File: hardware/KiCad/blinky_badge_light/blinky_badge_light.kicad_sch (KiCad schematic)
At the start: 14 parts, among them U1 ESP32-S3-WROOM-1

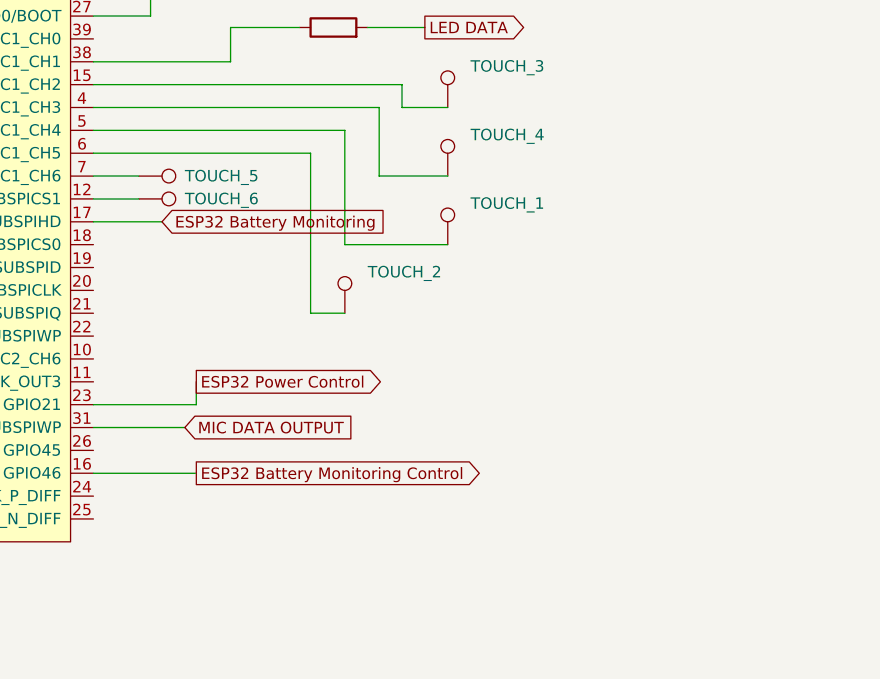
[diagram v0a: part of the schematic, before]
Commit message: adding a bunch of qs and annotated items on schematic
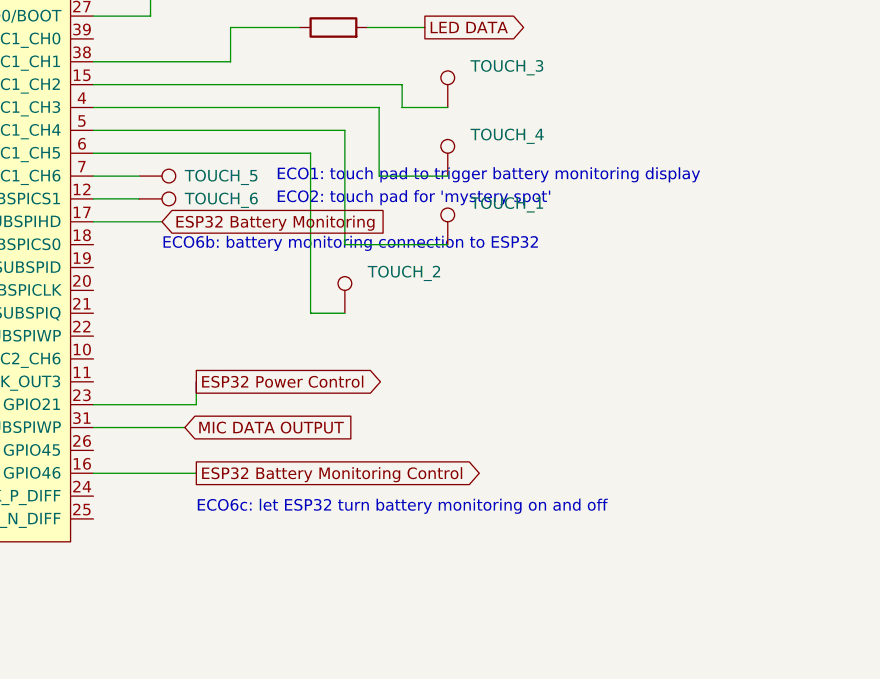
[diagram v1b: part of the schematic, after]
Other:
- note added: "ECO1: touch pad to trigger battery monitoring display"
- note added: "ECO2: touch pad for 'mystery spot'"
- note added: "ECO6b: battery monitoring connection to ESP32"
- note added: "ECO6c: let ESP32 turn battery monitoring on and off"
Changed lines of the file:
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@@
 	(generator_version "9.0")
 	(paper "A4")
+	(text "ECO2: touch pad for 'mystery spot'"
+		(exclude_from_sim yes)
+		(at 212.09 95.25 0)
+		(effects
+			(font
+				(size 1.27 1.27)
+				(color 119 0 255 1)
+			)
+			(justify left)
+		)
+	)
+	(text "ECO1: touch pad to trigger battery monitoring display"
+		(exclude_from_sim yes)
+		(at 212.09 92.71 0)
+		(effects
+			(font
+				(size 1.27 1.27)
+				(color 123 0 255 1)
+			)
+			(justify left)
+		)
+	)
+	(text "ECO6c: let ESP32 turn battery monitoring on and off\n"
+		(exclude_from_sim yes)
+		(at 203.2 129.54 0)
+		(effects
+			(font
+				(size 1.27 1.27)
+				(color 119 0 255 1)
+			)
+			(justify left)
+		)
+	)
+	(text "ECO6b: battery monitoring connection to ESP32"
+		(exclude_from_sim yes)
+		(at 199.39 100.33 0)
+		(effects
+			(font
+				(size 1.27 1.27)
+				(color 119 0 255 1)
+			)
+			(justify left)
+		)
+	)
 	(junction
 		(at 224.79 68.58)

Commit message: remove text from review
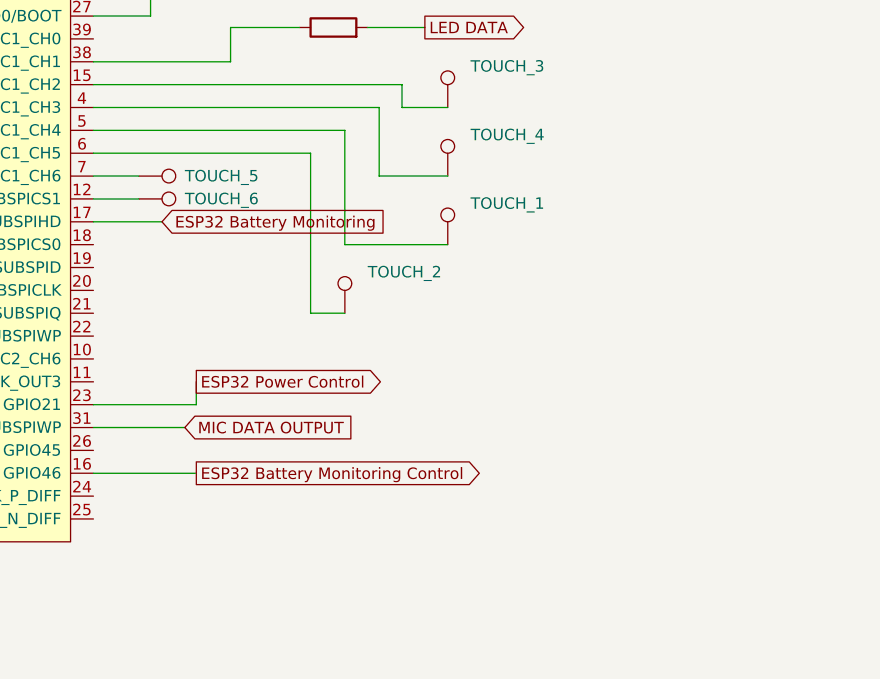
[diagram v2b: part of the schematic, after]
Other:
- note removed: "ECO1: touch pad to trigger battery monitoring display"
- note removed: "ECO2: touch pad for 'mystery spot'"
- note removed: "ECO6b: battery monitoring connection to ESP32"
- note removed: "ECO6c: let ESP32 turn battery monitoring on and off"
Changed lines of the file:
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@@
 	(generator_version "9.0")
 	(paper "A4")
-	(text "ECO2: touch pad for 'mystery spot'"
-		(exclude_from_sim yes)
-		(at 212.09 95.25 0)
-		(effects
-			(font
-				(size 1.27 1.27)
-				(color 119 0 255 1)
-			)
-			(justify left)
-		)
-	)
-	(text "ECO1: touch pad to trigger battery monitoring display"
-		(exclude_from_sim yes)
-		(at 212.09 92.71 0)
-		(effects
-			(font
-				(size 1.27 1.27)
-				(color 123 0 255 1)
-			)
-			(justify left)
-		)
-	)
-	(text "ECO6c: let ESP32 turn battery monitoring on and off\n"
-		(exclude_from_sim yes)
-		(at 203.2 129.54 0)
-		(effects
-			(font
-				(size 1.27 1.27)
-				(color 119 0 255 1)
-			)
-			(justify left)
-		)
-	)
-	(text "ECO6b: battery monitoring connection to ESP32"
-		(exclude_from_sim yes)
-		(at 199.39 100.33 0)
-		(effects
-			(font
-				(size 1.27 1.27)
-				(color 119 0 255 1)
-			)
-			(justify left)
-		)
-	)
 	(junction
 		(at 224.79 68.58)
